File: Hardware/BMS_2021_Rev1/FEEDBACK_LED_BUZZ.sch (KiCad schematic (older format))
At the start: 15 parts

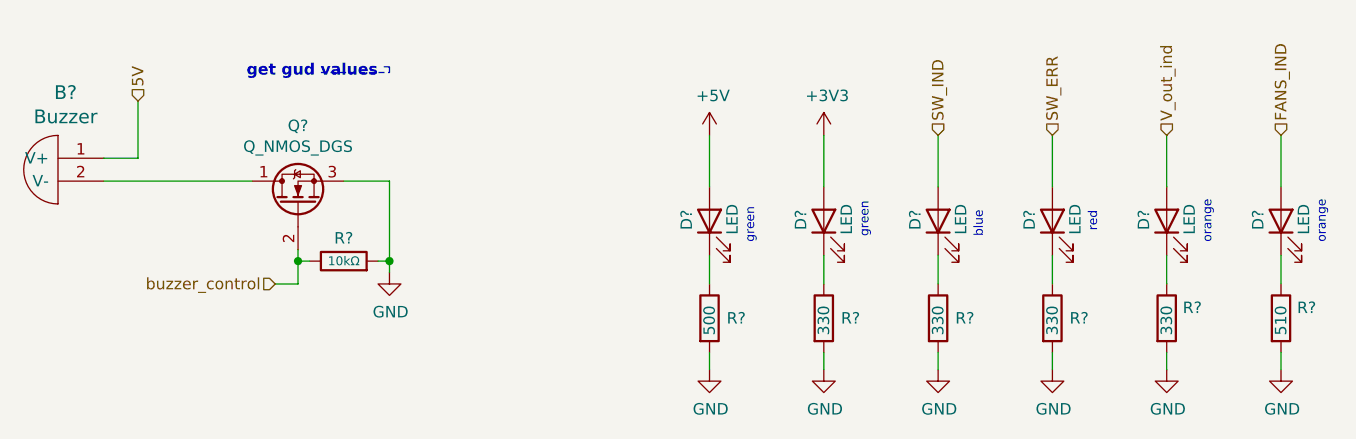
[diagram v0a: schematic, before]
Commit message: added libraries to docs folder
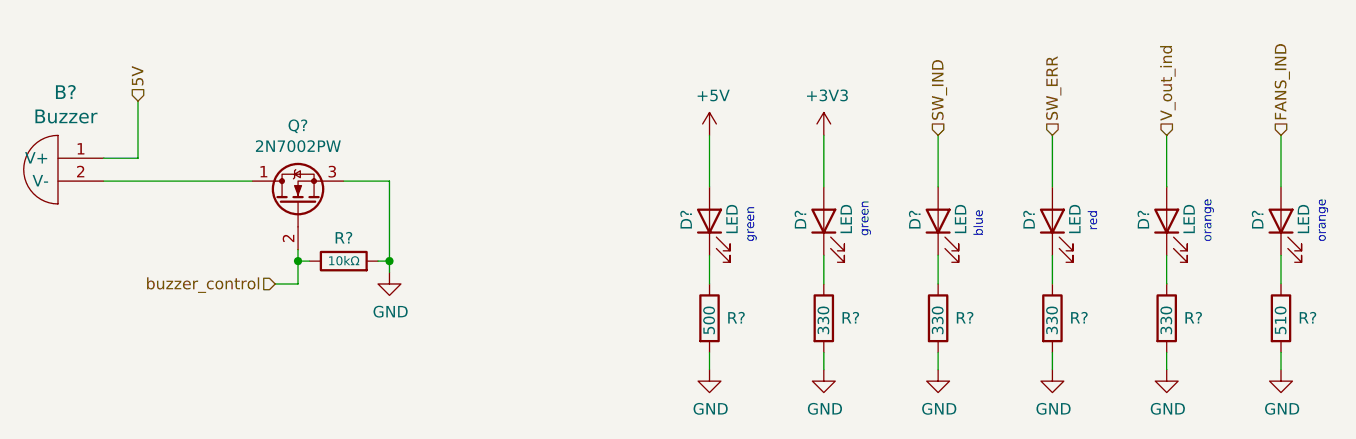
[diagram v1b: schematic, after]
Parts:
- Q?: value Q_NMOS_DGS -> 2N7002PW
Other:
- note removed: "get gud values\n"
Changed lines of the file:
@@
 AR Path="/5F80342B/5F88DE82" Ref="Q?"  Part="1"
 F 0 "Q?" V 3042 1800 50  0000 C CNN
-F 1 "Q_NMOS_DGS" V 2951 1800 50  0000 C CNN
+F 1 "2N7002PW" V 2951 1800 50  0000 C CNN
 F 2 "" H 2900 1900 50  0001 C CNN
-F 3 "~" H 2700 1800 50  0001 C CNN
+F 3 "https://www.digikey.com/en/products/detail/nexperia-usa-inc/2N7002PW-115/2531274" H 2700 1800 50  0001 C CNN
 	1    2700 1800
 	0    -1   -1   0
@@
 U 1 1 5F9CDBEE
 P 7000 2300
-F 0 "R?" H 7070 2346 50  0000 L CNN
+F 0 "R?" H 7075 2300 50  0000 L CNN
 F 1 "510" V 7000 2225 50  0000 L CNN
 F 2 "" V 6930 2300 50  0001 C CNN
@@
 U 1 1 5F9CCDEC
 P 6500 2300
-F 0 "R?" H 6570 2346 50  0000 L CNN
+F 0 "R?" H 6575 2300 50  0000 L CNN
 F 1 "330" V 6500 2225 50  0000 L CNN
 F 2 "" V 6430 2300 50  0001 C CNN
@@
 Text Notes 7200 1975 1    39   ~ 0
 orange
-Text Notes 2475 1250 0    50   ~ 10
-get gud values\n
-Wire Notes Line
-	2800 1225 3100 1225
-Wire Notes Line
-	3100 1225 3100 1200
-Wire Notes Line
-	3100 1200 3075 1200
-$Comp
-L Device:R R?
+$Comp
+L Device:R R?

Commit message: annotated sch.
some ICs got moved around- solve later
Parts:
- gave numbers to parts that had none: 15
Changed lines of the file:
@@
 $EndDescr
 $Comp
-L MRDT_Devices:Buzzer B?
+L MRDT_Devices:Buzzer B1
 U 1 1 5F88809B
 P 1650 1800
-F 0 "B?" H 1617 2287 60  0000 C CNN
+F 0 "B1" H 1617 2287 60  0000 C CNN
 F 1 "Buzzer" H 1617 2181 60  0000 C CNN
 F 2 "" H 1650 1800 60  0001 C CNN
@@
 P 2700 1800
 AR Path="/5F80341F/5F88DE82" Ref="Q?"  Part="1"
-AR Path="/5F80342B/5F88DE82" Ref="Q?"  Part="1"
-F 0 "Q?" V 3042 1800 50  0000 C CNN
+AR Path="/5F80342B/5F88DE82" Ref="Q5"  Part="1"
+F 0 "Q5" V 3042 1800 50  0000 C CNN
 F 1 "2N7002PW" V 2951 1800 50  0000 C CNN
 F 2 "" H 2900 1900 50  0001 C CNN
@@
 P 3100 2100
 AR Path="/5F80341F/5F88DE92" Ref="#PWR?"  Part="1"
-AR Path="/5F80342B/5F88DE92" Ref="#PWR?"  Part="1"
-F 0 "#PWR?" H 3100 1850 50  0001 C CNN
+AR Path="/5F80342B/5F88DE92" Ref="#PWR059"  Part="1"
+F 0 "#PWR059" H 3100 1850 50  0001 C CNN
 F 1 "GND" H 3105 1927 50  0000 C CNN
 F 2 "" H 3100 2100 50  0001 C CNN
@@
 P 2900 2050
 AR Path="/5F80341F/5F88DE98" Ref="R?"  Part="1"
-AR Path="/5F80342B/5F88DE98" Ref="R?"  Part="1"
-F 0 "R?" V 3000 2050 50  0000 C CNN
+AR Path="/5F80342B/5F88DE98" Ref="R47"  Part="1"
+F 0 "R47" V 3000 2050 50  0000 C CNN
 F 1 "10kΩ" V 2900 2050 39  0000 C CNN
 F 2 "" V 2830 2050 50  0001 C CNN
@@
 5V
 $Comp
-L power:+5V #PWR?
+L power:+5V #PWR060
 U 1 1 5F9C64C9
 P 4500 1500
-F 0 "#PWR?" H 4500 1350 50  0001 C CNN
+F 0 "#PWR060" H 4500 1350 50  0001 C CNN
 F 1 "+5V" H 4515 1673 50  0000 C CNN
 F 2 "" H 4500 1500 50  0001 C CNN
@@
 $EndComp
 $Comp
-L Device:LED D?
+L Device:LED D21
 U 1 1 5F9C73AB
 P 4500 1875
-F 0 "D?" H 4550 1975 50  0000 R CNN
+F 0 "D21" H 4550 1975 50  0000 R CNN
 F 1 "LED" H 4575 1775 50  0000 R CNN
 F 2 "" H 4500 1875 50  0001 C CNN
@@
 $EndComp
 $Comp
-L Device:R R?
+L Device:R R48
 U 1 1 5F9C7F4A
 P 4500 2300
-F 0 "R?" H 4575 2300 50  0000 L CNN
+F 0 "R48" H 4575 2300 50  0000 L CNN
 F 1 "500" V 4500 2225 50  0000 L CNN
 F 2 "" V 4430 2300 50  0001 C CNN
@@
 $EndComp
 $Comp
-L power:GND #PWR?
+L power:GND #PWR061
 U 1 1 5F9C82B5
 P 4500 2525
-F 0 "#PWR?" H 4500 2275 50  0001 C CNN
+F 0 "#PWR061" H 4500 2275 50  0001 C CNN
 F 1 "GND" H 4505 2352 50  0000 C CNN
 F 2 "" H 4500 2525 50  0001 C CNN
@@
 	7000 1725 7000 1500
 $Comp
-L power:GND #PWR?
+L power:GND #PWR067
 U 1 1 5F9CDBF4
 P 7000 2525
-F 0 "#PWR?" H 7000 2275 50  0001 C CNN
+F 0 "#PWR067" H 7000 2275 50  0001 C CNN
 F 1 "GND" H 7005 2352 50  0000 C CNN
 F 2 "" H 7000 2525 50  0001 C CNN
@@
 $EndComp
 $Comp
-L Device:R R?
+L Device:R R53
 U 1 1 5F9CDBEE
 P 7000 2300
-F 0 "R?" H 7075 2300 50  0000 L CNN
+F 0 "R53" H 7075 2300 50  0000 L CNN
 F 1 "510" V 7000 2225 50  0000 L CNN
 F 2 "" V 6930 2300 50  0001 C CNN
@@
 $EndComp
 $Comp
-L Device:LED D?
+L Device:LED D26
 U 1 1 5F9CDBE8
 P 7000 1875
-F 0 "D?" H 7050 1975 50  0000 R CNN
+F 0 "D26" H 7050 1975 50  0000 R CNN
 F 1 "LED" H 7075 1775 50  0000 R CNN
 F 2 "" H 7000 1875 50  0001 C CNN
@@
 	6500 1725 6500 1500
 $Comp
-L power:GND #PWR?
+L power:GND #PWR066
 U 1 1 5F9CCDF2
 P 6500 2525
-F 0 "#PWR?" H 6500 2275 50  0001 C CNN
+F 0 "#PWR066" H 6500 2275 50  0001 C CNN
 F 1 "GND" H 6505 2352 50  0000 C CNN
 F 2 "" H 6500 2525 50  0001 C CNN
@@
 $EndComp
 $Comp
-L Device:R R?
+L Device:R R52
 U 1 1 5F9CCDEC
 P 6500 2300
-F 0 "R?" H 6575 2300 50  0000 L CNN
+F 0 "R52" H 6575 2300 50  0000 L CNN
 F 1 "330" V 6500 2225 50  0000 L CNN
 F 2 "" V 6430 2300 50  0001 C CNN
@@
 $EndComp
 $Comp
-L Device:LED D?
+L Device:LED D25
 U 1 1 5F9CCDE6
 P 6500 1875
-F 0 "D?" H 6550 1975 50  0000 R CNN
+F 0 "D25" H 6550 1975 50  0000 R CNN
 F 1 "LED" H 6575 1775 50  0000 R CNN
 F 2 "" H 6500 1875 50  0001 C CNN
@@
 	6000 1725 6000 1500
 $Comp
-L power:GND #PWR?
+L power:GND #PWR065
 U 1 1 5F9CC21E
 P 6000 2525
-F 0 "#PWR?" H 6000 2275 50  0001 C CNN
+F 0 "#PWR065" H 6000 2275 50  0001 C CNN
 F 1 "GND" H 6005 2352 50  0000 C CNN
 F 2 "" H 6000 2525 50  0001 C CNN
@@
 $EndComp
 $Comp
-L Device:LED D?
+L Device:LED D24
 U 1 1 5F9CC212
 P 6000 1875
-F 0 "D?" H 6050 1975 50  0000 R CNN
+F 0 "D24" H 6050 1975 50  0000 R CNN
 F 1 "LED" H 6075 1775 50  0000 R CNN
 F 2 "" H 6000 1875 50  0001 C CNN
@@
 	5500 1725 5500 1500
 $Comp
-L power:GND #PWR?
+L power:GND #PWR064
 U 1 1 5F9CB51B
 P 5500 2525
-F 0 "#PWR?" H 5500 2275 50  0001 C CNN
+F 0 "#PWR064" H 5500 2275 50  0001 C CNN
 F 1 "GND" H 5505 2352 50  0000 C CNN
 F 2 "" H 5500 2525 50  0001 C CNN
@@
 $EndComp
 $Comp
-L Device:LED D?
+L Device:LED D23
 U 1 1 5F9CB50F
 P 5500 1875
-F 0 "D?" H 5550 1975 50  0000 R CNN
+F 0 "D23" H 5550 1975 50  0000 R CNN
 F 1 "LED" H 5575 1775 50  0000 R CNN
 F 2 "" H 5500 1875 50  0001 C CNN
@@
 	5000 1725 5000 1500
 $Comp
-L power:GND #PWR?
+L power:GND #PWR063
 U 1 1 5F9CA6A8
 P 5000 2525
-F 0 "#PWR?" H 5000 2275 50  0001 C CNN
+F 0 "#PWR063" H 5000 2275 50  0001 C CNN
 F 1 "GND" H 5005 2352 50  0000 C CNN
 F 2 "" H 5000 2525 50  0001 C CNN
@@
 $EndComp
 $Comp
-L Device:R R?
+L Device:R R49
 U 1 1 5F9CA6A2
 P 5000 2300
-F 0 "R?" H 5075 2300 50  0000 L CNN
+F 0 "R49" H 5075 2300 50  0000 L CNN
 F 1 "330" V 5000 2225 50  0000 L CNN
 F 2 "" V 4930 2300 50  0001 C CNN
@@
 $EndComp
 $Comp
-L Device:LED D?
+L Device:LED D22
 U 1 1 5F9CA69C
 P 5000 1875
-F 0 "D?" H 5050 1975 50  0000 R CNN
+F 0 "D22" H 5050 1975 50  0000 R CNN
 F 1 "LED" H 5075 1775 50  0000 R CNN
 F 2 "" H 5000 1875 50  0001 C CNN
@@
 SW_IND
 $Comp
-L power:+3V3 #PWR?
+L power:+3V3 #PWR062
 U 1 1 5F9C6840
 P 5000 1500
-F 0 "#PWR?" H 5000 1350 50  0001 C CNN
+F 0 "#PWR062" H 5000 1350 50  0001 C CNN
 F 1 "+3V3" H 5015 1673 50  0000 C CNN
 F 2 "" H 5000 1500 50  0001 C CNN
@@
 orange
 $Comp
-L Device:R R?
+L Device:R R50
 U 1 1 5FA7C5D8
 P 5500 2300
-F 0 "R?" H 5575 2300 50  0000 L CNN
+F 0 "R50" H 5575 2300 50  0000 L CNN
 F 1 "330" V 5500 2225 50  0000 L CNN
 F 2 "" V 5430 2300 50  0001 C CNN
@@
 $EndComp
 $Comp
-L Device:R R?
+L Device:R R51
 U 1 1 5FA7D082
 P 6000 2300
-F 0 "R?" H 6075 2300 50  0000 L CNN
+F 0 "R51" H 6075 2300 50  0000 L CNN
 F 1 "330" V 6000 2225 50  0000 L CNN
 F 2 "" V 5930 2300 50  0001 C CNN

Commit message: Began assigning footprints
Downloaded some footprint files from UltraLibrarian. Put in BMS_Hardware>Documentation> then copied files where they need to go
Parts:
- D21, D22, D23, D24, D25, D26: footprint (none) -> LED_SMD:LED_0603_1608Metric_Pad1.05x0.95mm_HandSolder
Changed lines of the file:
@@
 F 0 "D21" H 4550 1975 50  0000 R CNN
 F 1 "LED" H 4575 1775 50  0000 R CNN
-F 2 "" H 4500 1875 50  0001 C CNN
+F 2 "LED_SMD:LED_0603_1608Metric_Pad1.05x0.95mm_HandSolder" H 4500 1875 50  0001 C CNN
 F 3 "~" H 4500 1875 50  0001 C CNN
 	1    4500 1875
@@
 F 0 "D26" H 7050 1975 50  0000 R CNN
 F 1 "LED" H 7075 1775 50  0000 R CNN
-F 2 "" H 7000 1875 50  0001 C CNN
+F 2 "LED_SMD:LED_0603_1608Metric_Pad1.05x0.95mm_HandSolder" H 7000 1875 50  0001 C CNN
 F 3 "~" H 7000 1875 50  0001 C CNN
 	1    7000 1875
@@
 F 0 "D25" H 6550 1975 50  0000 R CNN
 F 1 "LED" H 6575 1775 50  0000 R CNN
-F 2 "" H 6500 1875 50  0001 C CNN
+F 2 "LED_SMD:LED_0603_1608Metric_Pad1.05x0.95mm_HandSolder" H 6500 1875 50  0001 C CNN
 F 3 "~" H 6500 1875 50  0001 C CNN
 	1    6500 1875
@@
 F 0 "D24" H 6050 1975 50  0000 R CNN
 F 1 "LED" H 6075 1775 50  0000 R CNN
-F 2 "" H 6000 1875 50  0001 C CNN
+F 2 "LED_SMD:LED_0603_1608Metric_Pad1.05x0.95mm_HandSolder" H 6000 1875 50  0001 C CNN
 F 3 "~" H 6000 1875 50  0001 C CNN
 	1    6000 1875
@@
 F 0 "D23" H 5550 1975 50  0000 R CNN
 F 1 "LED" H 5575 1775 50  0000 R CNN
-F 2 "" H 5500 1875 50  0001 C CNN
+F 2 "LED_SMD:LED_0603_1608Metric_Pad1.05x0.95mm_HandSolder" H 5500 1875 50  0001 C CNN
 F 3 "~" H 5500 1875 50  0001 C CNN
 	1    5500 1875
@@
 F 0 "D22" H 5050 1975 50  0000 R CNN
 F 1 "LED" H 5075 1775 50  0000 R CNN
-F 2 "" H 5000 1875 50  0001 C CNN
+F 2 "LED_SMD:LED_0603_1608Metric_Pad1.05x0.95mm_HandSolder" H 5000 1875 50  0001 C CNN
 F 3 "~" H 5000 1875 50  0001 C CNN
 	1    5000 1875

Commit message: more footprints added
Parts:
- B1: footprint (none) -> MRDT_Devices:BUZZER_SMI_1324_TW_5V_2_R
- R47, R48, R49, R50, R51, R52, R53: footprint (none) -> Resistor_SMD:R_0603_1608Metric_Pad1.05x0.95mm_HandSolder
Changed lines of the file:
@@
 F 0 "B1" H 1617 2287 60  0000 C CNN
 F 1 "Buzzer" H 1617 2181 60  0000 C CNN
-F 2 "" H 1650 1800 60  0001 C CNN
+F 2 "MRDT_Devices:BUZZER_SMI_1324_TW_5V_2_R" H 1650 1800 60  0001 C CNN
 F 3 "" H 1650 1800 60  0001 C CNN
 	1    1650 1800
@@
 F 0 "R47" V 3000 2050 50  0000 C CNN
 F 1 "10kΩ" V 2900 2050 39  0000 C CNN
-F 2 "" V 2830 2050 50  0001 C CNN
+F 2 "Resistor_SMD:R_0603_1608Metric_Pad1.05x0.95mm_HandSolder" V 2830 2050 50  0001 C CNN
 F 3 "~" H 2900 2050 50  0001 C CNN
 	1    2900 2050
@@
 F 0 "R48" H 4575 2300 50  0000 L CNN
 F 1 "500" V 4500 2225 50  0000 L CNN
-F 2 "" V 4430 2300 50  0001 C CNN
+F 2 "Resistor_SMD:R_0603_1608Metric_Pad1.05x0.95mm_HandSolder" V 4430 2300 50  0001 C CNN
 F 3 "~" H 4500 2300 50  0001 C CNN
 	1    4500 2300
@@
 F 0 "R53" H 7075 2300 50  0000 L CNN
 F 1 "510" V 7000 2225 50  0000 L CNN
-F 2 "" V 6930 2300 50  0001 C CNN
+F 2 "Resistor_SMD:R_0603_1608Metric_Pad1.05x0.95mm_HandSolder" V 6930 2300 50  0001 C CNN
 F 3 "~" H 7000 2300 50  0001 C CNN
 	1    7000 2300
@@
 F 0 "R52" H 6575 2300 50  0000 L CNN
 F 1 "330" V 6500 2225 50  0000 L CNN
-F 2 "" V 6430 2300 50  0001 C CNN
+F 2 "Resistor_SMD:R_0603_1608Metric_Pad1.05x0.95mm_HandSolder" V 6430 2300 50  0001 C CNN
 F 3 "~" H 6500 2300 50  0001 C CNN
 	1    6500 2300
@@
 F 0 "R49" H 5075 2300 50  0000 L CNN
 F 1 "330" V 5000 2225 50  0000 L CNN
-F 2 "" V 4930 2300 50  0001 C CNN
+F 2 "Resistor_SMD:R_0603_1608Metric_Pad1.05x0.95mm_HandSolder" V 4930 2300 50  0001 C CNN
 F 3 "~" H 5000 2300 50  0001 C CNN
 	1    5000 2300
@@
 F 0 "R50" H 5575 2300 50  0000 L CNN
 F 1 "330" V 5500 2225 50  0000 L CNN
-F 2 "" V 5430 2300 50  0001 C CNN
+F 2 "Resistor_SMD:R_0603_1608Metric_Pad1.05x0.95mm_HandSolder" V 5430 2300 50  0001 C CNN
 F 3 "~" H 5500 2300 50  0001 C CNN
 	1    5500 2300
@@
 F 0 "R51" H 6075 2300 50  0000 L CNN
 F 1 "330" V 6000 2225 50  0000 L CNN
-F 2 "" V 5930 2300 50  0001 C CNN
+F 2 "Resistor_SMD:R_0603_1608Metric_Pad1.05x0.95mm_HandSolder" V 5930 2300 50  0001 C CNN
 F 3 "~" H 6000 2300 50  0001 C CNN
 	1    6000 2300

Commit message: more footprints added
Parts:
- Q5: footprint (none) -> Package_TO_SOT_SMD:SOT-323_SC-70_Handsoldering
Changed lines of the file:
@@
 F 0 "Q5" V 3042 1800 50  0000 C CNN
 F 1 "2N7002PW" V 2951 1800 50  0000 C CNN
-F 2 "" H 2900 1900 50  0001 C CNN
+F 2 "Package_TO_SOT_SMD:SOT-323_SC-70_Handsoldering" H 2900 1900 50  0001 C CNN
 F 3 "https://www.digikey.com/en/products/detail/nexperia-usa-inc/2N7002PW-115/2531274" H 2700 1800 50  0001 C CNN
 	1    2700 1800
